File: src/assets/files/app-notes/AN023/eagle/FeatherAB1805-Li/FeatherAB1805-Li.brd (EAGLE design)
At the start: 50.8 x 22.9 mm, 11 parts, among them Q1 32.768kHz, Q2 2N7002L, U1 XC6215, U2 AB1805

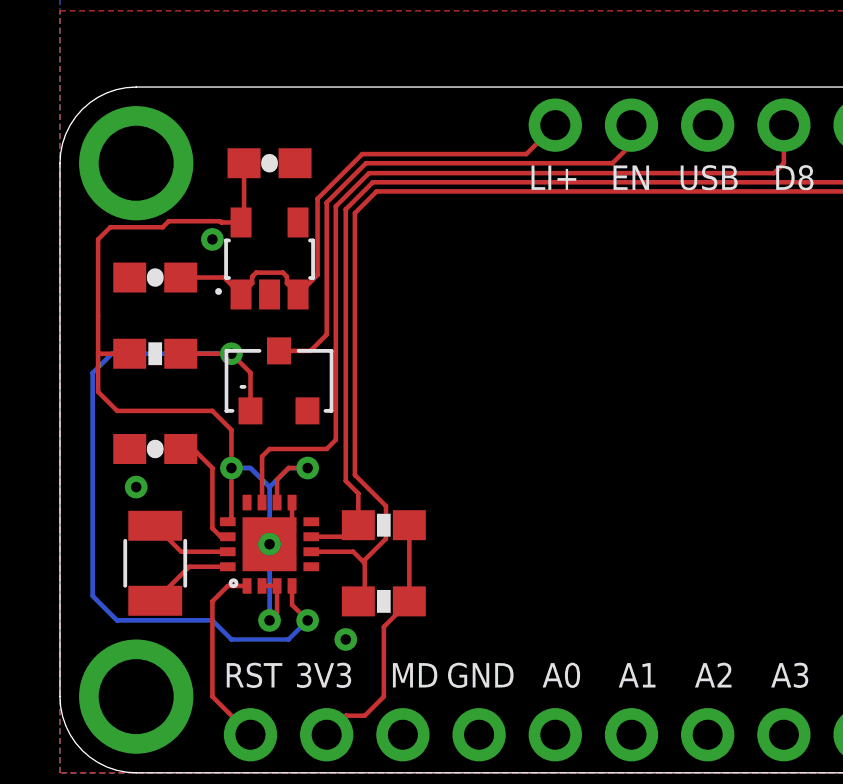
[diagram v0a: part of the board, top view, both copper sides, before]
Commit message: Update AB1805-Li design
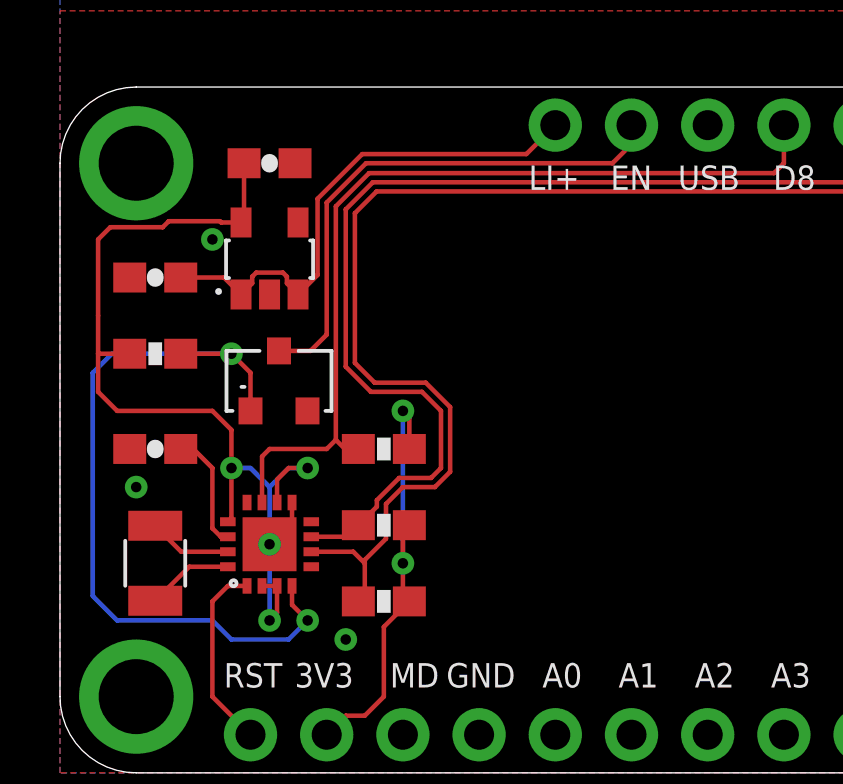
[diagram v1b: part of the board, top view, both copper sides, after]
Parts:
- added R1: 100K, rickk2:0603-RES
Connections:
- net 3V3: now also R1.2
- net D8: now also R1.1
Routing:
- net 3V3: track 8.50 -> 15.1 mm, vias 0 -> 2
- net SCL: track 46.7 -> 50.6 mm
- net SDA: track 52.3 -> 55.7 mm
- net D8: track 28.8 -> 29.7 mm
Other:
- board text added: "FeatherAB1805-Li v2"
- board text removed: "FeatherAB1805-Li v1"
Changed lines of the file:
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@@
 <text x="39.0144" y="19.431" size="0.8128" layer="21" font="vector" ratio="12">D2</text>
 <text x="45.085" y="3.175" size="1.016" layer="22" rot="MR0">FeatherAB1805-Li
-v1</text>
+v2</text>
 </plain>
 <attributes>
@@
 <attribute name="VALUE" x="5.685" y="16.595" size="0.4064" layer="51"/>
 </element>
+<element name="R1" library="rickk2" package="0603-RES" value="100K" x="10.795" y="10.795" smashed="yes">
+<attribute name="NAME" x="9.906" y="11.557" size="0.4064" layer="51" font="vector"/>
+<attribute name="VALUE" x="9.779" y="9.652" size="0.4064" layer="51" font="vector"/>
+</element>
 </elements>
 <signals>
@@
 <wire x1="8.89" y1="10.795" x2="9.1948" y2="11.0998" width="0.1524" layer="1"/>
 <wire x1="6.735" y1="9.01" x2="6.735" y2="10.545" width="0.1524" layer="1"/>
+<contactref element="R1" pad="1"/>
 <wire x1="9.1948" y1="11.0998" x2="9.1948" y2="18.8826875" width="0.1524" layer="1"/>
+<wire x1="9.945" y1="10.795" x2="9.4996" y2="10.795" width="0.1524" layer="1"/>
+<wire x1="9.4996" y1="10.795" x2="9.1948" y2="11.0998" width="0.1524" layer="1"/>
 </signal>
 <signal name="SCL">
@@
 <wire x1="41.275" y1="19.685" x2="41.91" y2="20.32" width="0.1524" layer="1"/>
 <wire x1="10.42816875" y1="19.685" x2="41.275" y2="19.685" width="0.1524" layer="1"/>
-<wire x1="9.945" y1="9.31" x2="9.945" y2="8.255" width="0.1524" layer="1"/>
-<wire x1="10.42816875" y1="19.685" x2="9.525" y2="18.78183125" width="0.1524" layer="1"/>
-<wire x1="9.525" y1="9.73" x2="9.945" y2="9.31" width="0.1524" layer="1"/>
-<wire x1="9.525" y1="18.78183125" x2="9.525" y2="9.73" width="0.1524" layer="1"/>
+<wire x1="9.525" y1="18.78183125" x2="10.42816875" y2="19.685" width="0.1524" layer="1"/>
+<wire x1="12.3698" y1="9.8298" x2="12.7" y2="10.16" width="0.1524" layer="1"/>
+<wire x1="12.7" y1="10.16" x2="12.7" y2="12.065" width="0.1524" layer="1"/>
+<wire x1="12.7" y1="12.065" x2="12.065" y2="12.7" width="0.1524" layer="1"/>
+<wire x1="9.945" y1="8.255" x2="10.5616" y2="8.8716" width="0.1524" layer="1"/>
+<wire x1="10.5616" y1="8.8716" x2="10.5616" y2="9.08765625" width="0.1524" layer="1"/>
+<wire x1="10.5616" y1="9.08765625" x2="11.30374375" y2="9.8298" width="0.1524" layer="1"/>
+<wire x1="11.30374375" y1="9.8298" x2="12.3698" y2="9.8298" width="0.1524" layer="1"/>
+<wire x1="10.36394375" y1="12.7" x2="9.525" y2="13.53894375" width="0.1524" layer="1"/>
+<wire x1="12.065" y1="12.7" x2="10.36394375" y2="12.7" width="0.1524" layer="1"/>
+<wire x1="9.525" y1="13.53894375" x2="9.525" y2="18.78183125" width="0.1524" layer="1"/>
 </signal>
 <signal name="SDA">
@@
 <contactref element="R3" pad="1"/>
 <contactref element="U2" pad="6"/>
-<wire x1="10.8664" y1="8.89" x2="10.8664" y2="7.8031125" width="0.1524" layer="1"/>
-<wire x1="10.8664" y1="8.89" x2="9.8298" y2="9.9266" width="0.1524" layer="1"/>
 <wire x1="41.6052" y1="19.3802" x2="41.91" y2="19.685" width="0.1524" layer="1"/>
 <wire x1="41.91" y1="19.685" x2="43.815" y2="19.685" width="0.1524" layer="1"/>
 <wire x1="43.815" y1="19.685" x2="44.45" y2="20.32" width="0.1524" layer="1"/>
 <wire x1="44.45" y1="20.32" x2="44.45" y2="21.59" width="0.1524" layer="1"/>
-<wire x1="9.8298" y1="9.9266" x2="9.8298" y2="18.655575" width="0.1524" layer="1"/>
 <wire x1="9.8298" y1="18.655575" x2="10.554425" y2="19.3802" width="0.1524" layer="1"/>
 <wire x1="10.554425" y1="19.3802" x2="41.6052" y2="19.3802" width="0.1524" layer="1"/>
@@
 <wire x1="10.16" y1="5.93" x2="9.945" y2="5.715" width="0.1524" layer="1"/>
 <wire x1="10.16" y1="7.0967125" x2="10.16" y2="6.985" width="0.1524" layer="1"/>
-<wire x1="10.8664" y1="7.8031125" x2="10.16" y2="7.0967125" width="0.1524" layer="1"/>
+<wire x1="10.16" y1="7.0967125" x2="10.8664" y2="7.8031125" width="0.1524" layer="1"/>
+<wire x1="10.8664" y1="8.9614" x2="11.43" y2="9.525" width="0.1524" layer="1"/>
+<wire x1="10.8664" y1="7.8031125" x2="10.8664" y2="8.9614" width="0.1524" layer="1"/>
+<wire x1="9.8298" y1="13.6652" x2="9.8298" y2="18.655575" width="0.1524" layer="1"/>
+<wire x1="12.49605625" y1="9.525" x2="13.0048" y2="10.03374375" width="0.1524" layer="1"/>
+<wire x1="13.0048" y1="10.03374375" x2="13.0048" y2="12.19125625" width="0.1524" layer="1"/>
+<wire x1="13.0048" y1="12.19125625" x2="12.19125625" y2="13.0048" width="0.1524" layer="1"/>
+<wire x1="10.4902" y1="13.0048" x2="9.8298" y2="13.6652" width="0.1524" layer="1"/>
+<wire x1="11.43" y1="9.525" x2="12.49605625" y2="9.525" width="0.1524" layer="1"/>
+<wire x1="12.19125625" y1="13.0048" x2="10.4902" y2="13.0048" width="0.1524" layer="1"/>
 </signal>
 <signal name="/RESET">
@@
 <contactref element="R2" pad="2"/>
 <contactref element="R3" pad="2"/>
-<wire x1="11.645" y1="5.715" x2="11.645" y2="8.255" width="0.1524" layer="1"/>
 <wire x1="8.89" y1="1.27" x2="9.525" y2="1.905" width="0.1524" layer="1"/>
 <wire x1="9.525" y1="1.905" x2="10.16" y2="1.905" width="0.1524" layer="1"/>
@@
 <wire x1="10.795" y1="4.865" x2="11.645" y2="5.715" width="0.1524" layer="1"/>
 <wire x1="10.795" y1="2.54" x2="10.795" y2="4.865" width="0.1524" layer="1"/>
+<contactref element="R1" pad="2"/>
+<via x="11.43" y="12.065" extent="1-16" drill="0.35"/>
+<via x="11.43" y="6.985" extent="1-16" drill="0.35"/>
+<wire x1="11.645" y1="5.715" x2="11.43" y2="5.93" width="0.1524" layer="1"/>
+<wire x1="11.43" y1="5.93" x2="11.43" y2="6.985" width="0.1524" layer="1"/>
+<wire x1="11.43" y1="6.985" x2="11.43" y2="8.04" width="0.1524" layer="1"/>
+<wire x1="11.43" y1="8.04" x2="11.645" y2="8.255" width="0.1524" layer="1"/>
+<wire x1="11.645" y1="10.795" x2="11.645" y2="11.85" width="0.1524" layer="1"/>
+<wire x1="11.645" y1="11.85" x2="11.43" y2="12.065" width="0.1524" layer="1"/>
+<wire x1="11.43" y1="12.065" x2="11.43" y2="6.985" width="0.1524" layer="16"/>
 </signal>
 <signal name="EN">
